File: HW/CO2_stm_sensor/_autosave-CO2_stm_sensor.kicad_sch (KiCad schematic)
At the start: 47 parts, among them IC1 SCD41-D-R2, IC2 TPS22917DBVR, IC3 TPS22917DBVR, J1 DM3D-SF(41), J2 SWD, J3 LP_UART, J4 DBG_UART, J5 BATTERY, J6 10118193-0001LF, U1 STM32L021K4T6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

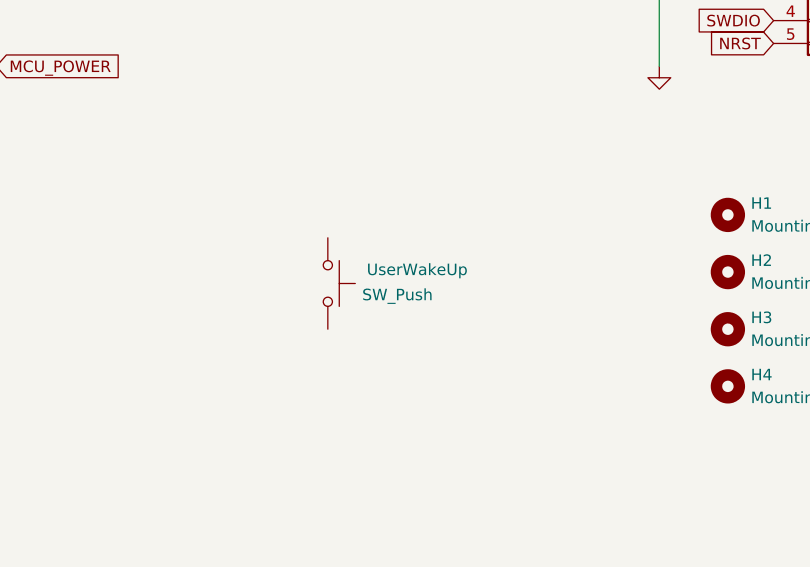
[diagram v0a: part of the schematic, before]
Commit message: setup firmware and _fw_gen folders
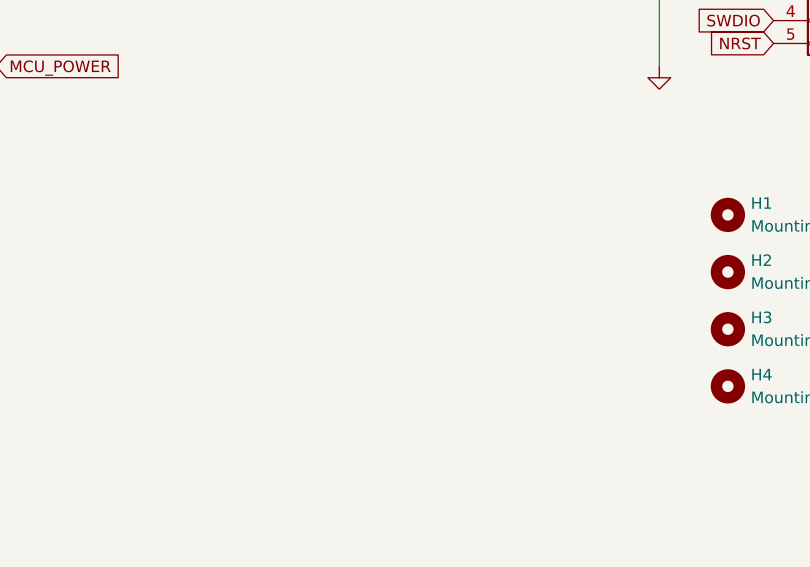
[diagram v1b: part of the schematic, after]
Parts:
- removed UserWakeUp: SW_Push, symbol Switch:SW_Push
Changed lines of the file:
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@@
-	)
-	(symbol
-		(lib_id "Switch:SW_Push")
-		(at 212.09 151.13 270)
-		(unit 1)
-		(exclude_from_sim no)
-		(in_bom yes)
-		(on_board yes)
-		(dnp no)
-		(property "Reference" "UserWakeUp"
-			(at 216.408 149.606 90)
-			(effects
-				(font
-					(size 1.27 1.27)
-				)
-				(justify left)
-			)
-		)
-		(property "Value" "SW_Push"
-			(at 215.9 152.3999 90)
-			(effects
-				(font
-					(size 1.27 1.27)
-				)
-				(justify left)
-			)
-		)
-		(property "Footprint" ""
-			(at 217.17 151.13 0)
-			(effects
-				(font
-					(size 1.27 1.27)
-				)
-				(hide yes)
-			)
-		)
-		(property "Datasheet" "~"
-			(at 217.17 151.13 0)
-			(effects
-				(font
-					(size 1.27 1.27)
-				)
-				(hide yes)
-			)
-		)
-		(property "Description" "Push button switch, generic, two pins"
-			(at 212.09 151.13 0)
-			(effects
-				(font
-					(size 1.27 1.27)
-				)
-				(hide yes)
-			)
-		)
-		(pin "2"
-		)
-		(pin "1"
-		)
-		(instances
-			(project ""
-				(path "/fbf6196a-da46-4b73-a741-a9cbb7111e74"
-					(reference "UserWakeUp")
-					(unit 1)
-				)
-			)
-		)
 	)
 	(symbol
